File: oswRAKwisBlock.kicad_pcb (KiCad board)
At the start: 2 copper layers, 33.8 x 46 mm, 31 parts, among them J1 WisBlock, J2 0524352471, J3 USB_B_Micro, Q1 SI1308EDL-T1-GE3, U1 MCP73811T-420I/OT

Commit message: Working on getting the placement settled.  VERY TIGHTgit pull!
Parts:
- added C11: 1u, AllardChip:CAPC100X50X60L25L, F.Cu at (135.6, 123.5)
- added J4: 10114830-10102LF, AllardConnFootPrints:AMPHENOL_10114830-10102LF, F.Cu at (122.3, 129.2)
- moved U1 4.85 mm to (127.3, 125.9)
- moved C10 4.73 mm to (127.2, 123.2)
- moved J3 4.10 mm to (131.7, 126.2)
- moved C9 1.06 mm to (135.2, 130.8), turned to -90 degrees
- moved L2 0.20 mm to (128.0, 133.1)
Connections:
- U1 pad 3: unconnected-(U1-V_{BAT}-Pad3) -> Net-(U1-V_{BAT})

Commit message: Adding a bunch of stuff to the design and some local models.
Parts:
- removed the REF** at (147.5, 127.0)
- added AN1: 1.575GHz ANT, AllardANT:MOLEX_1462350001_CHIP, F.Cu at (148.3, 102.3)
- added REF**: RAK11310, oswRAKlib:RAK11310, F.Cu at (136.9, 115.2)
- added REF**: 1.54 E-Paper Display, oswRAKlib:154_Epaper_Display, B.Cu at (136.8, 122.5)
- moved J4 29.1 mm to (148.9, 141.1), turned to 180 degrees
- moved C10 17.6 mm to (127.6, 140.9), turned to 90 degrees
- moved J3 16.6 mm to (124.0, 140.9)
- moved U1 15.2 mm to (130.2, 140.9), turned to 90 degrees
- moved R1 12.8 mm to (124.5, 127.6)
- moved S1 8.10 mm to (121.7, 129.8)
- moved C7 7.29 mm to (139.7, 140.5), turned to -90 degrees
- moved C5 6.58 mm to (137.7, 140.5), turned to -90 degrees
- moved C2 6.57 mm to (141.7, 140.5), turned to -90 degrees
- moved C4 6.48 mm to (138.7, 140.5), turned to -90 degrees
- moved C3 6.23 mm to (140.7, 140.5), turned to -90 degrees
- moved C6 6.13 mm to (132.8, 140.4), turned to -90 degrees
- moved S2 5.76 mm to (151.8, 131.8)
- moved C1 5.56 mm to (142.7, 140.5), turned to -90 degrees
- moved Q1 4.84 mm to (132.0, 127.9)
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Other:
- outline, holes or cut-outs redrawn
- copper layers 2 -> 4

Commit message: Working on the board a bit more.
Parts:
- removed J3: USB_B_Micro, AllardConnFootPrints:MOLEX_1051330011
- added J5: USB micro, AllardConnFootPrints:GCT_USB3190-GF-C, F.Cu at (123.5, 140.6)
- moved S1 2.20 mm to (121.8, 132.0)
- moved C8 1.02 mm to (126.0, 134.0)
- moved C10 0.96 mm to (127.3, 141.8), turned to 180 degrees
- moved S2 0.19 mm to (151.8, 132.0)

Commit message: Working on things.
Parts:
- moved C11 2.07 mm to (137.5, 121.1)
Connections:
- net Net-(J1-RESET) renamed /~{MCU_RES}
- net Net-(S1-K) renamed /BTN1
- net Net-(S2-K) renamed /BTN2
- J1 pad 3: unconnected-(J1-GND-Pad3) -> GND
- J1 pad 4: unconnected-(J1-GND-Pad4) -> GND
- J1 pad 6: unconnected-(J1-3V3-Pad6) -> VDD

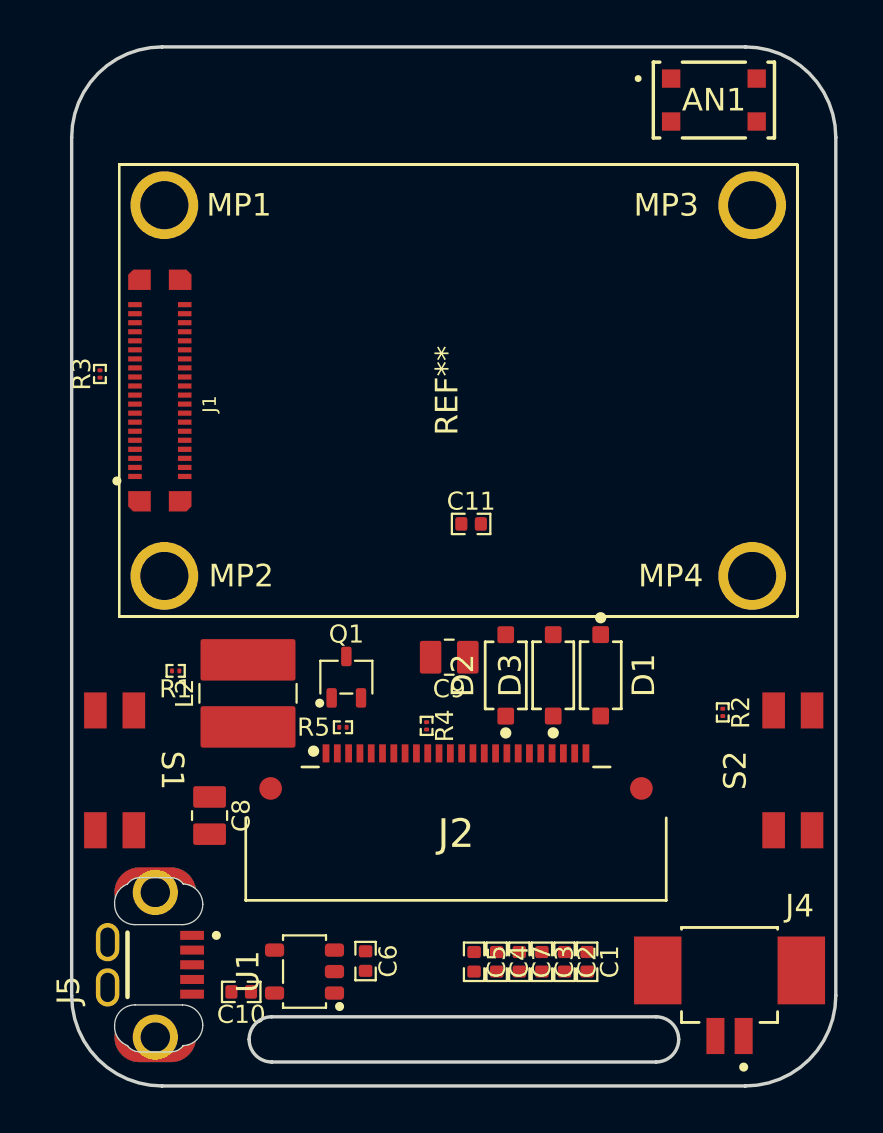
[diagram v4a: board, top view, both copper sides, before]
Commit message: Finally got the GPS chip wired in.  Just need to finish the pinout and then finalize the GPS part placement.
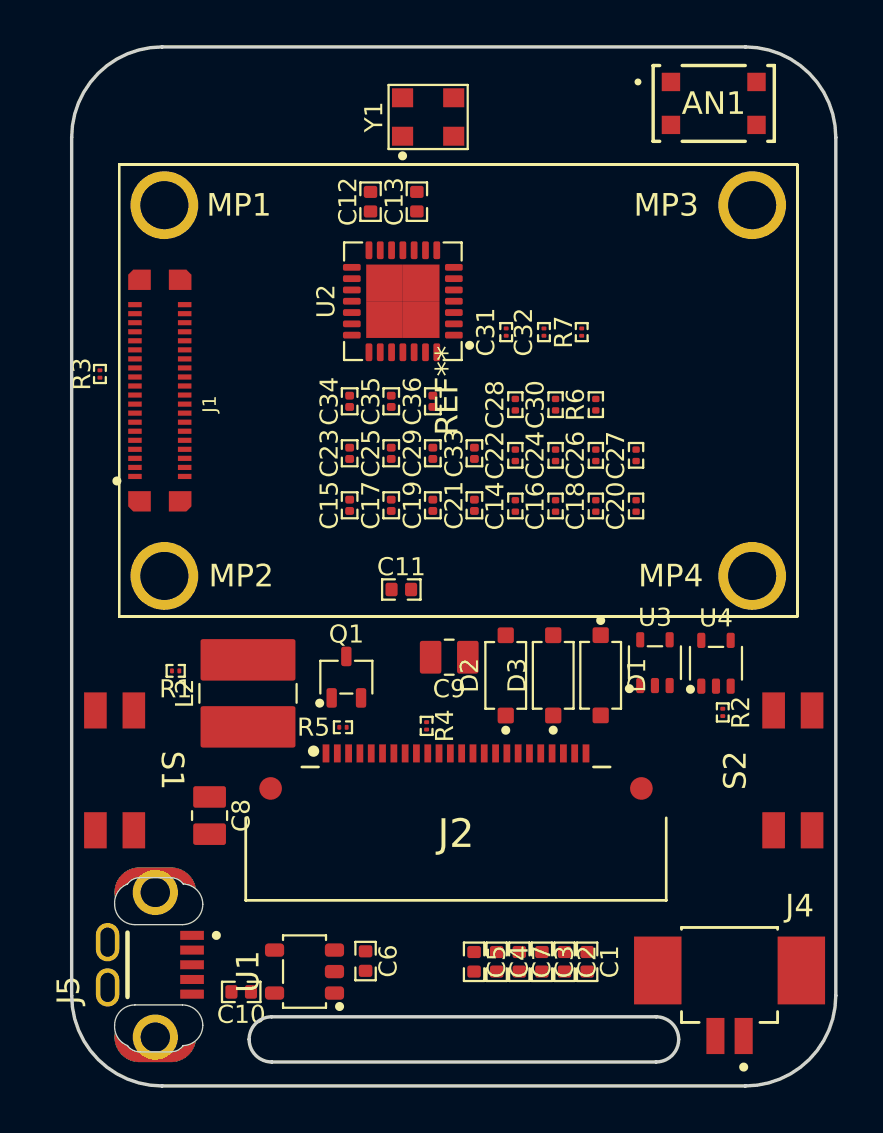
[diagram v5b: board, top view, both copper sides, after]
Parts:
- added C12: 1u, AllardChip:CAPC100X50X60L25L, F.Cu at (133.1, 106.8)
- added C13: 1u, AllardChip:CAPC100X50X60L25L, F.Cu at (135.1, 106.8)
- added C14: 100p, AllardChip:CAPC60X30X33L15L, F.Cu at (139.5, 120.3)
- added C15: 100n, AllardChip:CAPC60X30X39L17L, F.Cu at (132.1, 120.3)
- added C16: 100p, AllardChip:CAPC60X30X33L15L, F.Cu at (141.3, 120.3)
- added C17: 100n, AllardChip:CAPC60X30X39L17L, F.Cu at (134.0, 120.3)
- added C18: 100p, AllardChip:CAPC60X30X33L15L, F.Cu at (143.0, 120.3)
- added C19: 100n, AllardChip:CAPC60X30X39L17L, F.Cu at (135.8, 120.3)
- added C20: 100p, AllardChip:CAPC60X30X33L15L, F.Cu at (144.8, 120.3)
- added C21: 100n, AllardChip:CAPC60X30X39L17L, F.Cu at (137.7, 120.3)
- added C22: 100p, AllardChip:CAPC60X30X33L15L, F.Cu at (139.5, 118.1)
- added C23: 100n, AllardChip:CAPC60X30X39L17L, F.Cu at (132.1, 118.0)
- added C24: 100p, AllardChip:CAPC60X30X33L15L, F.Cu at (141.3, 118.1)
- added C25: 100n, AllardChip:CAPC60X30X39L17L, F.Cu at (134.0, 118.0)
- added C26: 27p, AllardChip:CAPC60X30X33L15L, F.Cu at (143.0, 118.1)
- added C27: 470p, AllardChip:CAPC60X30X33L15L, F.Cu at (144.8, 118.1)
- added C28: 6.8n, AllardChip:CAPC60X30X33L15L, F.Cu at (139.5, 115.8)
- added C29: 100n, AllardChip:CAPC60X30X39L17L, F.Cu at (135.8, 118.0)
- added C30: 470p, AllardChip:CAPC60X30X33L15L, F.Cu at (141.3, 115.8)
- added C31: 10n, AllardChip:CAPC40X20X22L10L, F.Cu at (139.1, 112.6)
- added C32: 10n, AllardChip:CAPC40X20X22L10L, F.Cu at (140.7, 112.6)
- added C33: 1uF, AllardChip:CAPC60X30X39L17L, F.Cu at (137.7, 118.0)
- added C34: 1uF, AllardChip:CAPC60X30X39L17L, F.Cu at (132.1, 115.7)
- added C35: 1uF, AllardChip:CAPC60X30X39L17L, F.Cu at (134.0, 115.7)
- added C36: 1uF, AllardChip:CAPC60X30X39L17L, F.Cu at (135.8, 115.7)
- added R6: 20k, AllardChip:RESC60X30X26L15L, F.Cu at (143.0, 115.8)
- added R7: 10k, AllardChip:RESC40X20X15L10L, F.Cu at (142.4, 112.6)
- added U2: MAX2769B, Allard_dfn_qfn:QFN29P50_500X500X80L55X25T325L, F.Cu at (134.5, 111.2)
- added U3: MAX8510EXK29+T, AllardSOT:SOT23-5P65_210X110L42X22L, F.Cu at (145.7, 127.2)
- added U4: MAX8510EXK29+T, AllardSOT:SOT23-5P65_210X110L42X22L, F.Cu at (148.3, 127.3)
- added Y1: TXETCDSANF-16.368000, Allard_dfn_qfn:OSCDFN4_250X320X100L70X80L, F.Cu at (135.6, 103.1)
- D1, D2, D3: footprint AllardSOD:SOD370X155X135L32X57N -> AllardSOD:SOD370X155X135L32X57L
- moved C11 4.23 mm to (134.4, 124.0)
- moved AN1 0.15 mm to (148.2, 102.5)
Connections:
- AN1 pad 4: unconnected-(AN1-FD-Pad4) -> Net-(AN1-FD)
